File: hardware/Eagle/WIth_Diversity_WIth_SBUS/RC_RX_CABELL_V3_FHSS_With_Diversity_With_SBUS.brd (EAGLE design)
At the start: 32.4 x 66 mm, 19 parts, among them IC1 AMS1117 3V3, M2 NRF24L01

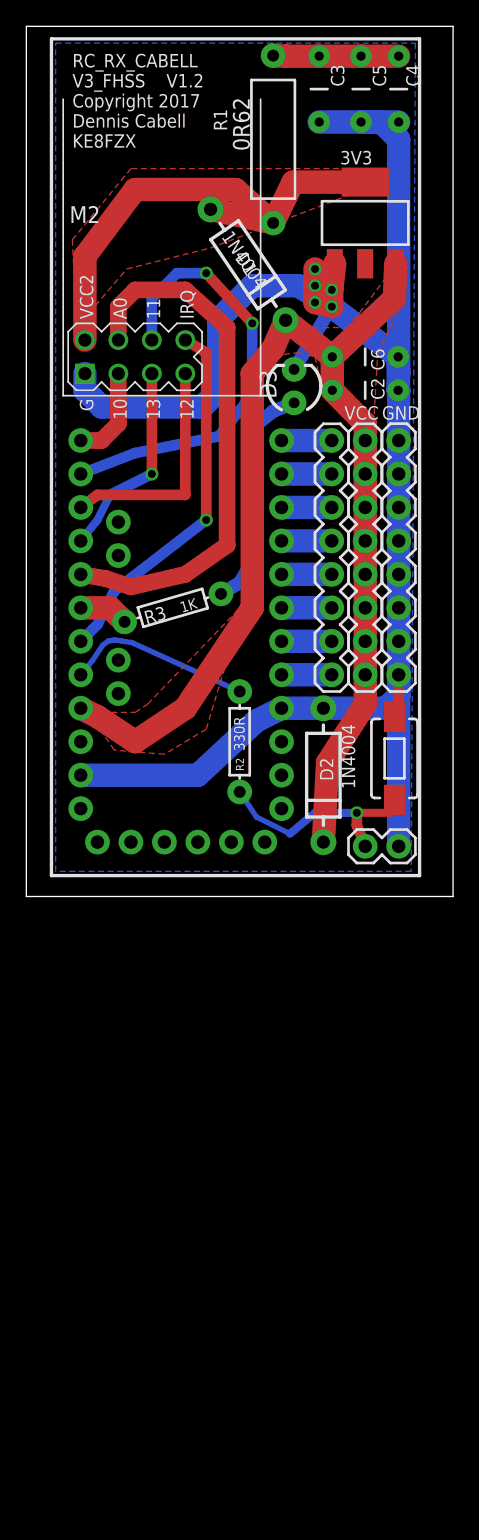
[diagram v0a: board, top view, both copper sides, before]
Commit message: Hardware Updates for SBUS & PPM
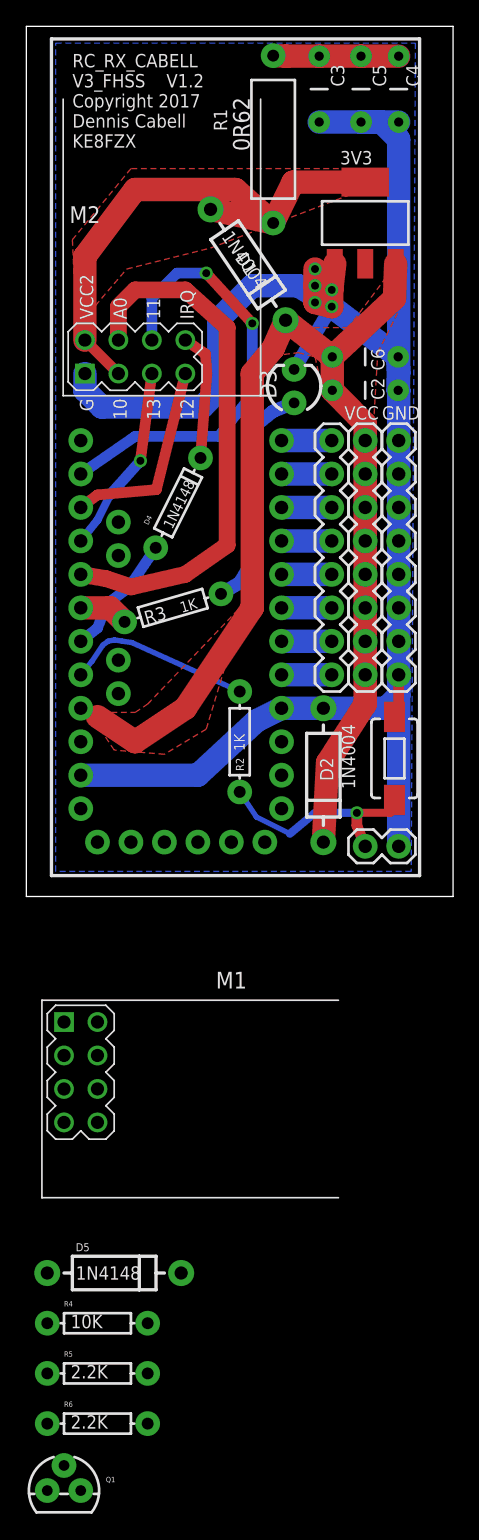
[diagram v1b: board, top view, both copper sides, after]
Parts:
- added D4: 1N4148, SparkFun-DiscreteSemi:DIODE-1N4148
- added D5: 1N4148, SparkFun-DiscreteSemi:DIODE-1N4001
- added M1: NRF24L01, diy-modules:WIRELESS-NRF24L01
- added Q1: 2N3904, SparkFun-DiscreteSemi:TO-92
- added R4: 10K, SparkFun-Passives:AXIAL-0.3
- added R5, R6: 2.2K, SparkFun-Passives:AXIAL-0.3
- R2: value 330R -> 1K
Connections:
- new net 3.3V: Q1.1
- new net N$16: D4.C, M2.8
- new net N$17: D5.C, M1.8
- new net N$23: M1.4, U$2.13
- new net S.BUS_OUTPUT: Q1.3, R5.P$2
- new net SERIAL_SIG: Q1.2, R6.P$2
- net 5V: now also R4.P$2, R5.P$1
- net GND: now also M1.1
- net N$1: now also R4.P$1
- net N$13: now also D4.A, D5.A; no longer M2.8
- net N$15: now also M1.5
- net N$20: now also M1.6
- net N$22: now also M1.7
- net N$3: now also R6.P$1, U$2.1; no longer M2.3, U$2.13
- net VCC: now also M1.2, M1.3, M2.3
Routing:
- net N$13: track 28.0 -> 9.30 mm, vias 1 -> 0
- net N$16: track 0.00 -> 9.77 mm
- net N$3: track 7.19 -> 0.00 mm
- net VCC: track 37.9 -> 41.5 mm
- net N$22: track 17.5 -> 15.2 mm
- net 5V: track 93.5 -> 92.1 mm
- net N$15: track 15.3 -> 14.3 mm
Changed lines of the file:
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@@
 <attribute name="VALUE" x="39.37" y="15.5575" size="0.8128" layer="27"/>
 </element>
-<element name="R2" library="SparkFun-Passives" package="AXIAL-0.3" value="330R" x="48.895" y="21.2725" smashed="yes" rot="R90">
+<element name="R2" library="SparkFun-Passives" package="AXIAL-0.3" value="1K" x="48.895" y="21.2725" smashed="yes" rot="R90">
 <attribute name="NAME" x="49.2125" y="19.05" size="0.6096" layer="25" font="vector" ratio="15" rot="R90"/>
 <attribute name="VALUE" x="49.276" y="20.574" size="0.8128" layer="21" font="vector" ratio="15" rot="R90"/>
@@
 <element name="JP1" library="SparkFun-Connectors" package="1X02" value="Bind Jumper" x="60.96" y="13.335" smashed="yes" rot="R180">
 <attribute name="VALUE" x="59.69" y="12.065" size="0.6096" layer="27" rot="R180"/>
+</element>
+<element name="D4" library="SparkFun-DiscreteSemi" package="DIODE-1N4148" value="1N4148" x="44.22" y="39.4" rot="R63.5"/>
+<element name="M1" library="diy-modules" package="WIRELESS-NRF24L01" value="NRF24L01" x="48.26" y="-6.35"/>
+<element name="D5" library="SparkFun-DiscreteSemi" package="DIODE-1N4001" value="1N4148" x="39.37" y="-19.05"/>
+<element name="R4" library="SparkFun-Passives" package="AXIAL-0.3" value="10K" x="38.1" y="-22.86"/>
+<element name="R5" library="SparkFun-Passives" package="AXIAL-0.3" value="2.2K" x="38.1" y="-26.67"/>
+<element name="R6" library="SparkFun-Passives" package="AXIAL-0.3" value="2.2K" x="38.1" y="-30.48"/>
+<element name="Q1" library="SparkFun-DiscreteSemi" package="TO-92" value="2N3904" x="35.56" y="-35.56">
+<attribute name="PROD_ID" value="TRANS-08447" x="35.56" y="-35.56" size="1.778" layer="27" display="off"/>
 </element>
 </elements>
@@
 <contactref element="JP1" pad="1"/>
 <wire x1="60.96" y1="13.335" x2="60.96" y2="26.3525" width="1.778" layer="16"/>
+<contactref element="M1" pad="1"/>
+<wire x1="36.83" y1="18.7325" x2="35.56" y2="0" width="0" layer="19" extent="1-1"/>
 </signal>
 <signal name="5V">
@@
 <wire x1="52.37804375" y1="53.260953125" x2="51.435" y2="51.1175" width="1.778" layer="1"/>
 <wire x1="51.435" y1="51.1175" x2="49.8475" y2="49.2125" width="1.778" layer="1"/>
-<contactref element="U$2" pad="21"/>
 <wire x1="40.9575" y1="21.2725" x2="38.1" y2="23.1775" width="1.778" layer="1"/>
-<wire x1="38.1" y1="23.1775" x2="36.83" y2="23.8125" width="1.778" layer="1"/>
 <wire x1="58.42" y1="24.13" x2="55.5625" y2="19.685" width="1.778" layer="1"/>
 <wire x1="55.5625" y1="19.685" x2="55.245" y2="13.6525" width="1.778" layer="1"/>
@@
 <vertex x="40.9575" y="23.495"/>
 </polygon>
+<contactref element="U$2" pad="21"/>
+<contactref element="R4" pad="P$2"/>
+<contactref element="R5" pad="P$1"/>
+<wire x1="36.83" y1="23.8125" x2="38.1" y2="23.1775" width="0" layer="19" extent="1-1"/>
+<wire x1="41.91" y1="-22.86" x2="55.245" y2="13.6525" width="0" layer="19" extent="1-1"/>
+<wire x1="34.29" y1="-26.67" x2="41.91" y2="-22.86" width="0" layer="19" extent="1-1"/>
 </signal>
 <signal name="N$14">
@@
 <contactref element="R1" pad="P$2"/>
 <wire x1="51.435" y1="73.3425" x2="52.4275" y2="73.3025" width="1.778" layer="1"/>
-</signal>
-<signal name="N$3">
-<contactref element="M2" pad="3"/>
-<wire x1="38.4175" y1="44.1325" x2="39.6875" y2="45.4025" width="1.27" layer="1"/>
-<wire x1="39.6875" y1="45.4025" x2="39.6875" y2="49.2125" width="1.27" layer="1"/>
-<contactref element="U$2" pad="13"/>
-<wire x1="38.4175" y1="44.1325" x2="36.83" y2="44.1325" width="1.27" layer="1"/>
 </signal>
 <signal name="N$18">
@@
 <contactref element="M2" pad="5"/>
 <contactref element="U$2" pad="16"/>
-<wire x1="42.2275" y1="49.2125" x2="42.2275" y2="41.5925" width="0.8128" layer="1"/>
-<wire x1="42.2275" y1="41.5925" x2="39.0525" y2="40.005" width="0.8128" layer="16"/>
+<wire x1="42.2275" y1="49.2125" x2="41.3575" y2="42.5925" width="0.8128" layer="1"/>
+<wire x1="41.3575" y1="42.5925" x2="39.0525" y2="40.005" width="0.8128" layer="16"/>
 <wire x1="39.0525" y1="40.005" x2="38.1" y2="38.1" width="0.6096" layer="16"/>
 <wire x1="38.1" y1="38.1" x2="36.83" y2="36.5125" width="0.6096" layer="16"/>
-<via x="42.2275" y="41.5925" extent="1-16" drill="0.6" shape="square"/>
+<via x="41.3575" y="42.5925" extent="1-16" drill="0.6" shape="square"/>
+<contactref element="M1" pad="5"/>
+<wire x1="35.56" y1="-5.08" x2="36.83" y2="36.5125" width="0" layer="19" extent="1-1"/>
 </signal>
 <signal name="N$20">
 <contactref element="M2" pad="6"/>
 <contactref element="U$2" pad="14"/>
-<wire x1="36.83" y1="41.5925" x2="40.9575" y2="43.18" width="0.8128" layer="16"/>
-<wire x1="40.9575" y1="43.18" x2="47.3075" y2="44.45" width="0.8128" layer="16"/>
+<wire x1="36.83" y1="41.5925" x2="40.9575" y2="44.45" width="0.8128" layer="16"/>
+<wire x1="40.9575" y1="44.45" x2="47.3075" y2="44.45" width="0.8128" layer="16"/>
 <wire x1="47.3075" y1="44.45" x2="49.8475" y2="47.625" width="0.8128" layer="16"/>
 <wire x1="49.8475" y1="47.625" x2="49.8475" y2="53.0225" width="0.8128" layer="16"/>
@@
 <via x="49.8475" y="53.0225" extent="1-16" drill="0.6" shape="square"/>
 <via x="46.355" y="56.8325" extent="1-16" drill="0.6" shape="square"/>
+<contactref element="M1" pad="6"/>
+<wire x1="38.1" y1="-5.08" x2="36.83" y2="41.5925" width="0" layer="19" extent="1-1"/>
 </signal>
 <signal name="N$22">
 <contactref element="M2" pad="7"/>
 <contactref element="U$2" pad="15"/>
-<wire x1="44.7675" y1="49.2125" x2="44.7675" y2="40.005" width="0.8128" layer="1"/>
-<wire x1="44.7675" y1="40.005" x2="38.1" y2="40.005" width="0.8128" layer="1"/>
+<wire x1="44.7675" y1="49.2125" x2="42.5675" y2="40.405" width="0.8128" layer="1"/>
+<wire x1="42.5675" y1="40.405" x2="38.1" y2="40.005" width="0.8128" layer="1"/>
 <wire x1="38.1" y1="40.005" x2="36.83" y2="39.0525" width="0.8128" layer="1"/>
+<contactref element="M1" pad="7"/>
+<wire x1="35.56" y1="-7.62" x2="36.83" y2="39.0525" width="0" layer="19" extent="1-1"/>
 </signal>
 <signal name="N$13">
 <contactref element="U$2" pad="19"/>
-<contactref element="M2" pad="8"/>
-<wire x1="36.83" y1="28.8925" x2="38.1" y2="30.1625" width="0.8128" layer="16"/>
-<wire x1="38.1" y1="30.1625" x2="39.37" y2="32.7025" width="0.8128" layer="16"/>
-<wire x1="39.37" y1="32.7025" x2="46.355" y2="38.1" width="0.8128" layer="16"/>
-<wire x1="46.355" y1="38.1" x2="46.355" y2="50.8" width="0.8128" layer="1"/>
-<wire x1="46.355" y1="50.8" x2="44.7675" y2="51.7525" width="0.8128" layer="1"/>
-<via x="46.355" y="38.1" extent="1-16" drill="0.6" shape="square"/>
+<contactref element="D4" pad="A"/>
+<contactref element="D5" pad="A"/>
+<wire x1="42.519984375" y1="35.9903" x2="40.5" y2="33" width="0.8128" layer="16"/>
+<wire x1="40.5" y1="33" x2="38.8" y2="31.7" width="0.8128" layer="16"/>
+<wire x1="38.8" y1="31.7" x2="38.1" y2="29.9" width="0.8128" layer="16"/>
+<wire x1="38.1" y1="29.9" x2="36.83" y2="28.8925" width="0.8128" layer="16"/>
+<wire x1="34.29" y1="-19.05" x2="36.83" y2="28.8925" width="0" layer="19" extent="1-1"/>
 </signal>
 <signal name="N$21">
@@
 <contactref element="U$2" pad="5"/>
 <wire x1="55.88" y1="26.3525" x2="52.07" y2="26.3525" width="1.778" layer="16"/>
+<contactref element="R4" pad="P$1"/>
+<wire x1="34.29" y1="-22.86" x2="52.07" y2="26.3525" width="0" layer="19" extent="1-1"/>
 </signal>
 <signal name="N$5">
@@
 <vertex x="57.4675" y="62.865"/>
 </polygon>
+<contactref element="M2" pad="3"/>
+<contactref element="M1" pad="2"/>
+<contactref element="M1" pad="3"/>
+<wire x1="37.1475" y1="51.7525" x2="39.6875" y2="49.2125" width="0.8128" layer="1"/>
+<wire x1="35.56" y1="-2.54" x2="38.1" y2="0" width="0" layer="19" extent="1-1"/>
+<wire x1="39.6875" y1="49.2125" x2="38.1" y2="0" width="0" layer="19" extent="1-1"/>
 </signal>
 <signal name="N$12">
@@
 <wire x1="57.785" y1="14.9225" x2="58.42" y2="13.335" width="0.8128" layer="1"/>
 </signal>
+<signal name="N$16">
+<contactref element="D4" pad="C"/>
+<contactref element="M2" pad="8"/>
+<wire x1="45.9200125" y1="42.809696875" x2="46.4" y2="49.2" width="0.8128" layer="1"/>
+<wire x1="46.4" y1="49.2" x2="46.3" y2="50.7" width="0.8128" layer="1"/>
+<wire x1="46.3" y1="50.7" x2="44.7675" y2="51.7525" width="0.8128" layer="1"/>
+</signal>
+<signal name="N$17">
+<contactref element="D5" pad="C"/>
+<contactref element="M1" pad="8"/>
+<wire x1="44.45" y1="-19.05" x2="38.1" y2="-7.62" width="0" layer="19" extent="1-1"/>
+</signal>
+<signal name="N$23">
+<contactref element="M1" pad="4"/>
+<contactref element="U$2" pad="13"/>
+<wire x1="38.1" y1="-2.54" x2="36.83" y2="44.1325" width="0" layer="19" extent="1-1"/>
+</signal>
+<signal name="N$3">
+<contactref element="U$2" pad="1"/>
+<contactref element="R6" pad="P$1"/>
+<wire x1="34.29" y1="-30.48" x2="52.07" y2="16.1925" width="0" layer="19" extent="1-1"/>
+</signal>
+<signal name="SERIAL_SIG">
+<contactref element="R6" pad="P$2"/>
+<contactref element="Q1" pad="2"/>
+<wire x1="35.56" y1="-33.655" x2="41.91" y2="-30.48" width="0" layer="19" extent="1-1"/>
+</signal>
+<signal name="3.3V">
+<contactref element="Q1" pad="1"/>
+</signal>
+<signal name="S.BUS_OUTPUT">
+<contactref element="R5" pad="P$2"/>
+<contactref element="Q1" pad="3"/>
+<wire x1="36.83" y1="-35.56" x2="41.91" y2="-26.67" width="0" layer="19" extent="1-1"/>
+</signal>
 </signals>
